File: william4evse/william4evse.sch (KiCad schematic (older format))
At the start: 2 parts, among them J1 Boom_Precision_RJ45-B-1x1, U1 RCMB121

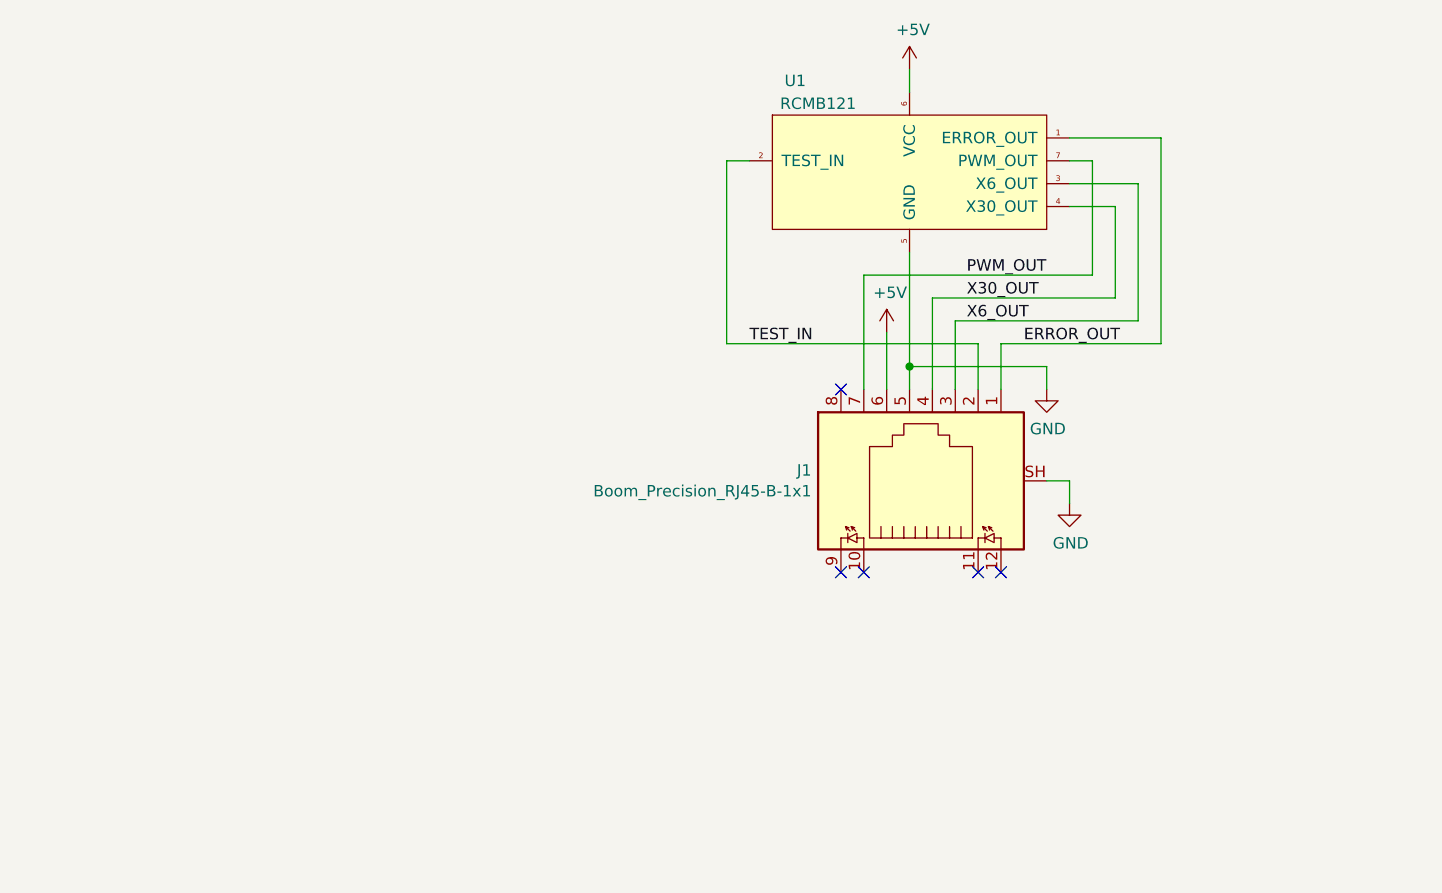
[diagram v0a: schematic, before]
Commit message: william: Add err_out relay output
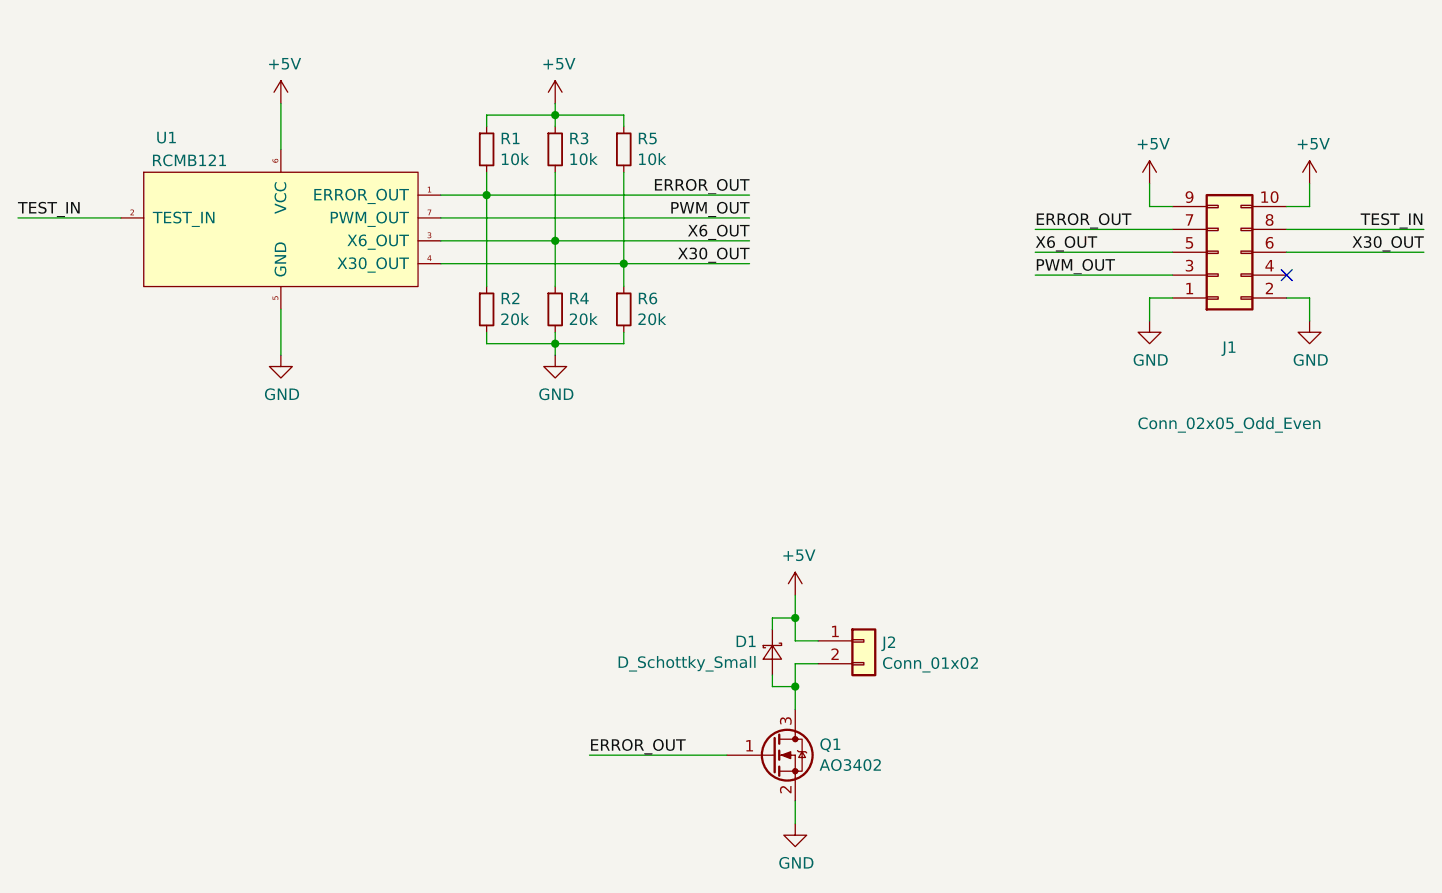
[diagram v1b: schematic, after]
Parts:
- removed J1: Boom_Precision_RJ45-B-1x1, Connector_RJ:RJ45_Amphenol_RJHSE538X, symbol ma4evse:Boom_Precision_RJ45-B-1x1
- added D1: D_Schottky_Small, Diode_SMD:D_SOD-123, symbol Device:D_Schottky_Small
- added J1: Conn_02x05_Odd_Even, Connector_PinHeader_2.54mm:PinHeader_2x05_P2.54mm_Horizontal, symbol Connector_Generic:Conn_02x05_Odd_Even
- added J2: Conn_01x02, Connector_JST:JST_PH_B2B-PH-K_1x02_P2.00mm_Vertical, symbol Connector_Generic:Conn_01x02
- added Q1: AO3402, Package_TO_SOT_SMD:SOT-23, symbol ma4evse:AO3402
- added R1, R3, R5: 10k, Resistor_SMD:R_0603_1608Metric, symbol Device:R_Small
- added R2, R4, R6: 20k, Resistor_SMD:R_0603_1608Metric, symbol Device:R_Small
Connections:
- net +5V: now also D1.1 (K), J1.10 (Pin_10), J1.9 (Pin_9), J2.1 (Pin_1), R1.1, R3.1, R5.1
- net ERROR_OUT: now also J1.7 (Pin_7), Q1.1 (G), R1.2, R2.1
- net GND: now also J1.1 (Pin_1), J1.2 (Pin_2), Q1.2 (S), R2.2, R4.2, R6.2
- net PWM_OUT: now also J1.3 (Pin_3)
- net TEST_IN: now also J1.8 (Pin_8)
- net X30_OUT: now also J1.6 (Pin_6), R5.2, R6.1
- net X6_OUT: now also J1.5 (Pin_5), R3.2, R4.1
- new net: D1.2 (A), J2.2 (Pin_2), Q1.3 (D)
- no-connect marks 5 -> 1
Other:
- moved on the sheet: U1

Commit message: william: Revert "Add err_out relay output"
This reverts commit fe4c97044222ea82c6b882aa488b85d2dc32cb0e.
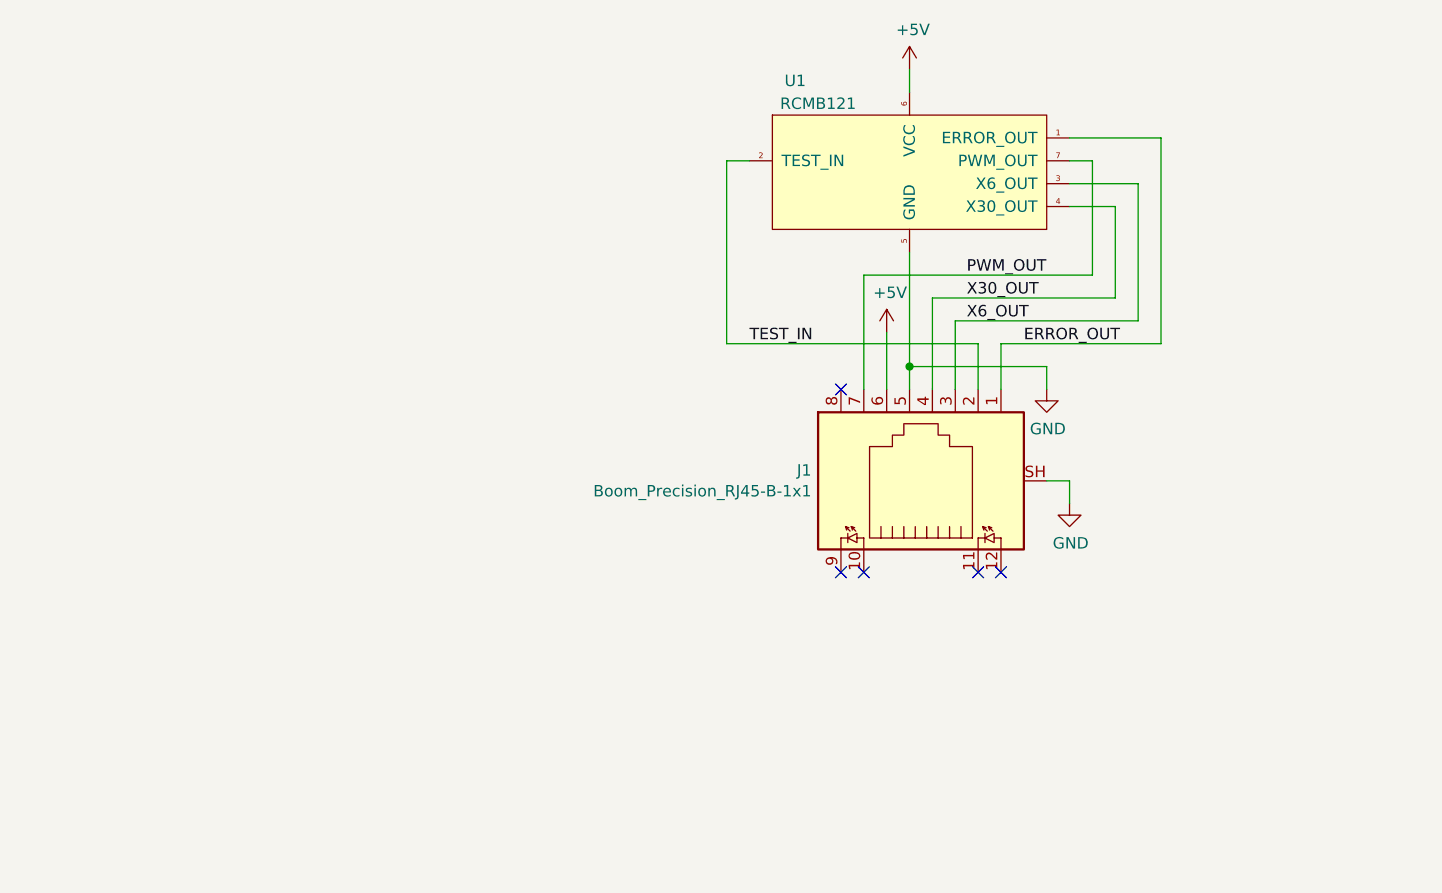
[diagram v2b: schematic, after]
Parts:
- removed D1: D_Schottky_Small, Diode_SMD:D_SOD-123, symbol Device:D_Schottky_Small
- removed J1: Conn_02x05_Odd_Even, Connector_PinHeader_2.54mm:PinHeader_2x05_P2.54mm_Horizontal, symbol Connector_Generic:Conn_02x05_Odd_Even
- removed J2: Conn_01x02, Connector_JST:JST_PH_B2B-PH-K_1x02_P2.00mm_Vertical, symbol Connector_Generic:Conn_01x02
- removed Q1: AO3402, Package_TO_SOT_SMD:SOT-23, symbol ma4evse:AO3402
- removed R1, R3, R5: 10k, Resistor_SMD:R_0603_1608Metric, symbol Device:R_Small
- removed R2, R4, R6: 20k, Resistor_SMD:R_0603_1608Metric, symbol Device:R_Small
- added J1: Boom_Precision_RJ45-B-1x1, Connector_RJ:RJ45_Amphenol_RJHSE538X, symbol ma4evse:Boom_Precision_RJ45-B-1x1
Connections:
- net +5V: now also J1.6
- net ERROR_OUT: now also J1.1
- net GND: now also J1.5, J1.SH
- net PWM_OUT: now also J1.7
- net TEST_IN: now also J1.2
- net X30_OUT: now also J1.4
- net X6_OUT: now also J1.3
- no-connect marks 1 -> 5
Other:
- moved on the sheet: U1
